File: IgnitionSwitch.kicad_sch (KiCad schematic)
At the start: 13 parts, among them J28 KILL_SW_IND, J7 BPS_PWR_OUT, J9 POW_2ND_CONN, SW8 SW_Rotary2x6, U5 EL3H7, U6 EL3H7

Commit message: Remove 12V isolator, swap CAN connector pins, etc.
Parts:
- SW8: footprint UTSVT_Special:CK1035_resized -> (none)
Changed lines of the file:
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@@
     (effects (font (size 1.27 1.27)) (justify left))
   )
-  (symbol (lib_id "Switch:SW_Rotary2x6") (at 163.83 96.52 180)
+  (symbol (lib_id "Switch:SW_Rotary2x6") (at 163.83 96.52 180) (unit 1)
     (in_bom yes) (on_board yes)
     (property "Reference" "SW8" (id 0) (at 162.56 75.565 0))
     (property "Value" "SW_Rotary2x6" (id 1) (at 162.56 77.8764 0))
-    (property "Footprint" "UTSVT_Special:CK1035_resized" (id 2) (at 166.37 111.76 0)
+    (property "Footprint" "" (id 2) (at 166.37 111.76 0)
       (effects (font (size 1.27 1.27)) hide)
     )
@@
     (pin "9")
   )
-  (symbol (lib_id "Device:R_US") (at 231.14 113.03 0)
+  (symbol (lib_id "Device:R_US") (at 231.14 113.03 0) (unit 1)
     (in_bom yes) (on_board yes)
     (property "Reference" "R12" (id 0) (at 232.8672 111.8616 0)
@@
     (pin "2")
   )
-  (symbol (lib_id "Device:LED") (at 231.14 121.92 90)
+  (symbol (lib_id "Device:LED") (at 231.14 121.92 90) (unit 1)
     (in_bom yes) (on_board yes)
     (property "Reference" "D1" (id 0) (at 234.1372 120.9294 90)
@@
     (pin "2")
   )
-  (symbol (lib_id "Connector:TestPoint") (at 137.16 82.55 0)
+  (symbol (lib_id "Connector:TestPoint") (at 137.16 82.55 0) (unit 1)
     (in_bom yes) (on_board yes)
     (property "Reference" "TP10" (id 0) (at 138.6332 79.5528 0)
@@
     (pin "1")
   )
-  (symbol (lib_id "Isolator:SFH617A-1") (at 100.33 99.06 270)
+  (symbol (lib_id "Isolator:SFH617A-1") (at 100.33 99.06 270) (unit 1)
     (in_bom yes) (on_board yes)
     (property "Reference" "U5" (id 0) (at 105.1052 97.8916 90)
@@
     (pin "4")
   )
-  (symbol (lib_id "Isolator:SFH617A-1") (at 123.19 99.06 270)
+  (symbol (lib_id "Isolator:SFH617A-1") (at 123.19 99.06 270) (unit 1)
     (in_bom yes) (on_board yes)
     (property "Reference" "U6" (id 0) (at 127.9652 97.8916 90)
@@
     (pin "4")
   )
-  (symbol (lib_id "power:GNDPWR") (at 114.3 92.71 0)
+  (symbol (lib_id "power:GNDPWR") (at 114.3 92.71 0) (unit 1)
     (in_bom yes) (on_board yes)
     (property "Reference" "#PWR0145" (id 0) (at 114.3 97.79 0)
@@
     (pin "1")
   )
-  (symbol (lib_id "power:GNDPWR") (at 91.44 92.71 0)
+  (symbol (lib_id "power:GNDPWR") (at 91.44 92.71 0) (unit 1)
     (in_bom yes) (on_board yes)
     (property "Reference" "#PWR0146" (id 0) (at 91.44 97.79 0)
@@
     (pin "1")
   )
-  (symbol (lib_id "power:GND") (at 120.65 106.68 0)
+  (symbol (lib_id "power:GND") (at 120.65 106.68 0) (unit 1)
     (in_bom yes) (on_board yes)
     (property "Reference" "#PWR0147" (id 0) (at 120.65 113.03 0)
@@
     (pin "1")
   )
-  (symbol (lib_id "power:GND") (at 97.79 106.68 0)
+  (symbol (lib_id "power:GND") (at 97.79 106.68 0) (unit 1)
     (in_bom yes) (on_board yes)
     (property "Reference" "#PWR0148" (id 0) (at 97.79 113.03 0)
@@
     (pin "1")
   )
-  (symbol (lib_id "Device:R_US") (at 106.68 113.03 0)
+  (symbol (lib_id "Device:R_US") (at 106.68 113.03 0) (unit 1)
     (in_bom yes) (on_board yes)
     (property "Reference" "R10" (id 0) (at 108.4072 111.8616 0)
@@
     (pin "2")
   )
-  (symbol (lib_id "Device:R_US") (at 129.54 113.03 0)
+  (symbol (lib_id "Device:R_US") (at 129.54 113.03 0) (unit 1)
     (in_bom yes) (on_board yes)
     (property "Reference" "R11" (id 0) (at 131.2672 111.8616 0)
@@
     (pin "2")
   )
-  (symbol (lib_id "power:+3.3V") (at 129.54 109.22 0)
+  (symbol (lib_id "power:+3.3V") (at 129.54 109.22 0) (unit 1)
     (in_bom yes) (on_board yes)
     (property "Reference" "#PWR0149" (id 0) (at 129.54 113.03 0)
@@
     (pin "1")
   )
-  (symbol (lib_id "power:+3.3V") (at 106.68 109.22 0)
+  (symbol (lib_id "power:+3.3V") (at 106.68 109.22 0) (unit 1)
     (in_bom yes) (on_board yes)
     (property "Reference" "#PWR0150" (id 0) (at 106.68 113.03 0)
@@
     (pin "1")
   )
-  (symbol (lib_id "Connector_Generic:Conn_01x02") (at 175.26 120.65 0)
+  (symbol (lib_id "Connector_Generic:Conn_01x02") (at 175.26 120.65 0) (unit 1)
     (in_bom yes) (on_board yes)
     (property "Reference" "J7" (id 0) (at 177.292 120.8532 0)
@@
     (pin "2")
   )
-  (symbol (lib_id "power:GNDPWR") (at 167.64 124.46 0)
+  (symbol (lib_id "power:GNDPWR") (at 167.64 124.46 0) (unit 1)
     (in_bom yes) (on_board yes)
     (property "Reference" "#PWR0151" (id 0) (at 167.64 129.54 0)
@@
     (pin "1")
   )
-  (symbol (lib_id "Connector_Generic:Conn_01x02") (at 255.27 106.68 0)
+  (symbol (lib_id "Connector_Generic:Conn_01x02") (at 255.27 106.68 0) (unit 1)
     (in_bom yes) (on_board yes)
     (property "Reference" "J28" (id 0) (at 257.302 106.8832 0)
@@
     (pin "2")
   )
-  (symbol (lib_id "Connector_Generic:Conn_01x02") (at 191.77 93.98 0)
+  (symbol (lib_id "Connector_Generic:Conn_01x02") (at 191.77 93.98 0) (unit 1)
     (in_bom yes) (on_board yes)
     (property "Reference" "J9" (id 0) (at 193.802 94.1832 0)
@@
     (pin "2")
   )
-  (symbol (lib_id "power:GNDPWR") (at 184.15 99.06 0)
+  (symbol (lib_id "power:GNDPWR") (at 184.15 99.06 0) (unit 1)
     (in_bom yes) (on_board yes)
     (property "Reference" "#PWR0129" (id 0) (at 184.15 104.14 0)
@@
     (pin "1")
   )
-  (symbol (lib_id "Device:R_US") (at 135.89 88.9 270)
+  (symbol (lib_id "Device:R_US") (at 135.89 88.9 270) (unit 1)
     (in_bom yes) (on_board yes)
     (property "Reference" "R6" (id 0) (at 137.0584 90.6272 0)
@@
     (pin "2")
   )
-  (symbol (lib_id "Device:R_US") (at 111.506 86.36 270)
+  (symbol (lib_id "Device:R_US") (at 111.506 86.36 270) (unit 1)
     (in_bom yes) (on_board yes)
     (property "Reference" "R5" (id 0) (at 112.6744 88.0872 0)

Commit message: Release v2.4 and gerbers
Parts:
- SW8: footprint (none) -> Connector_Molex:Molex_Micro-Fit_3.0_43045-1412_2x07_P3.00mm_Vertical
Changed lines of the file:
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@@
     (property "Reference" "SW8" (id 0) (at 162.56 75.565 0))
     (property "Value" "SW_Rotary2x6" (id 1) (at 162.56 77.8764 0))
-    (property "Footprint" "" (id 2) (at 166.37 111.76 0)
+    (property "Footprint" "Connector_Molex:Molex_Micro-Fit_3.0_43045-1412_2x07_P3.00mm_Vertical" (id 2) (at 166.37 111.76 0)
       (effects (font (size 1.27 1.27)) hide)
     )

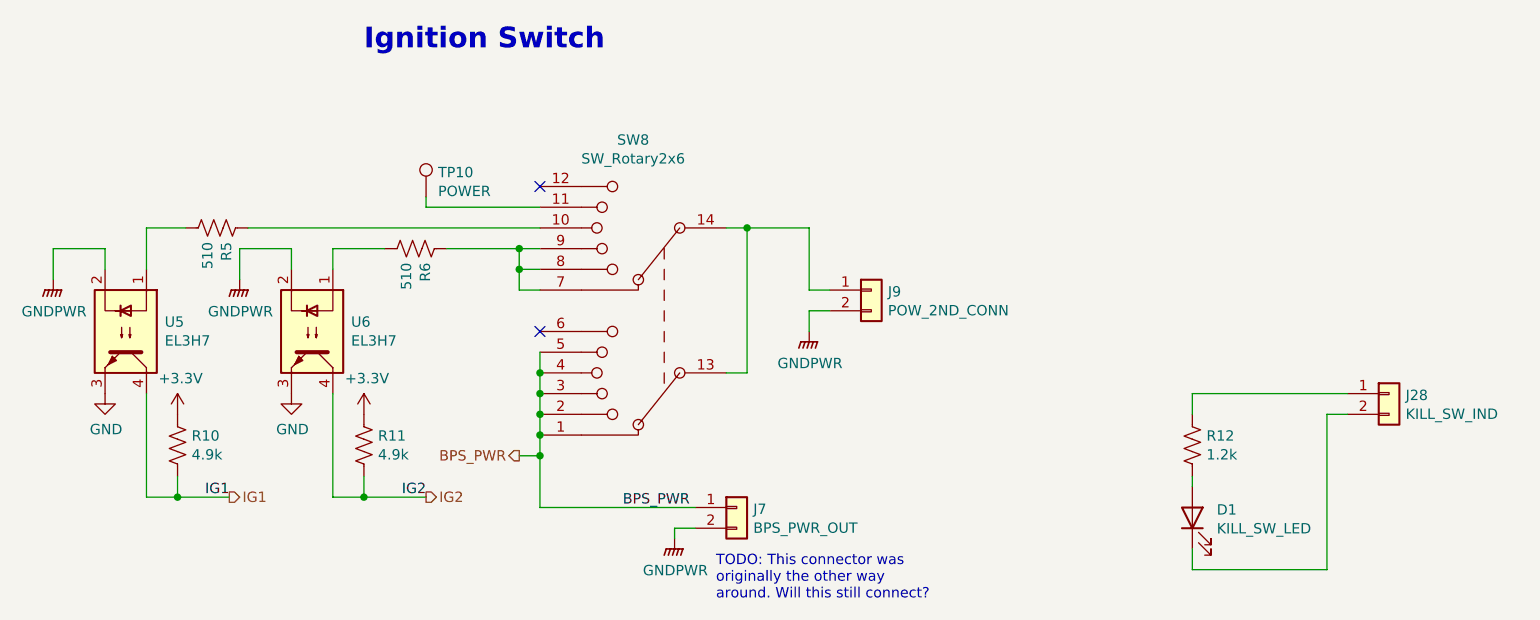
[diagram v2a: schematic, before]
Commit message: Daybreak rework (#24)
* Schematic notations for rework changes

* Updated schematic in accordance to previous weeks annotated changes

* Added .lck files to .gitignore.

* Renamed Clk to PA5, removed CAN_TX/RX test points, deleted other .lck file and #auto_saved_files# (hopefully this does not break anything.

* Changed testpoints to pin headers.

* removed camera, fixed connectors, and changed status LEDS

* Schematic finished :) hopefully not broken

* Added back lights + drivers + timer for all blinkers and brake lights

* Fuse added for motorCAN 12V

* Renamed local net labels to be different from hierarchical ones in the MinionBrdInterface so that they aren't connected. Changed Regen input to BPS Hazard light since we aren't using regen but will be alerting the driver of BPS faults.

* Flipped optoisolators, changed resistor values, added second connector to motor can and disconnected shield pins for now since I haven't seen them used (will chack against old version to see what the circuit looked like), copied power-in circuit from contactor board, added optoisolator to timer and blinker light connection.

* Changed names and added power flags until KiCAD ERC was satisfied. Hopefully this did not involve doing anything that wasn't supposed to be done.

* Added UTSVT libraries to the gitignore.

* Added footprints. I think this is everything except the fuse.

* Fuse footprint added and blinker changed to software

* Started cleaning some comments, changed EL3H7 data sheet link, removed extra motor CAN connector and changed original one to match (I think) motor controller connector, removed extra mounting holes, removed hierarchical power labels.

* renamed power state indicators to contactors and removed unused contactors, added current limiting resistors to lights drivers, changed mosfet to new mosfet

* Updated contactor pins.

* added circuitry for limit switch brake, added mosfet to drive LEDs, cleaned up legacy comments, 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
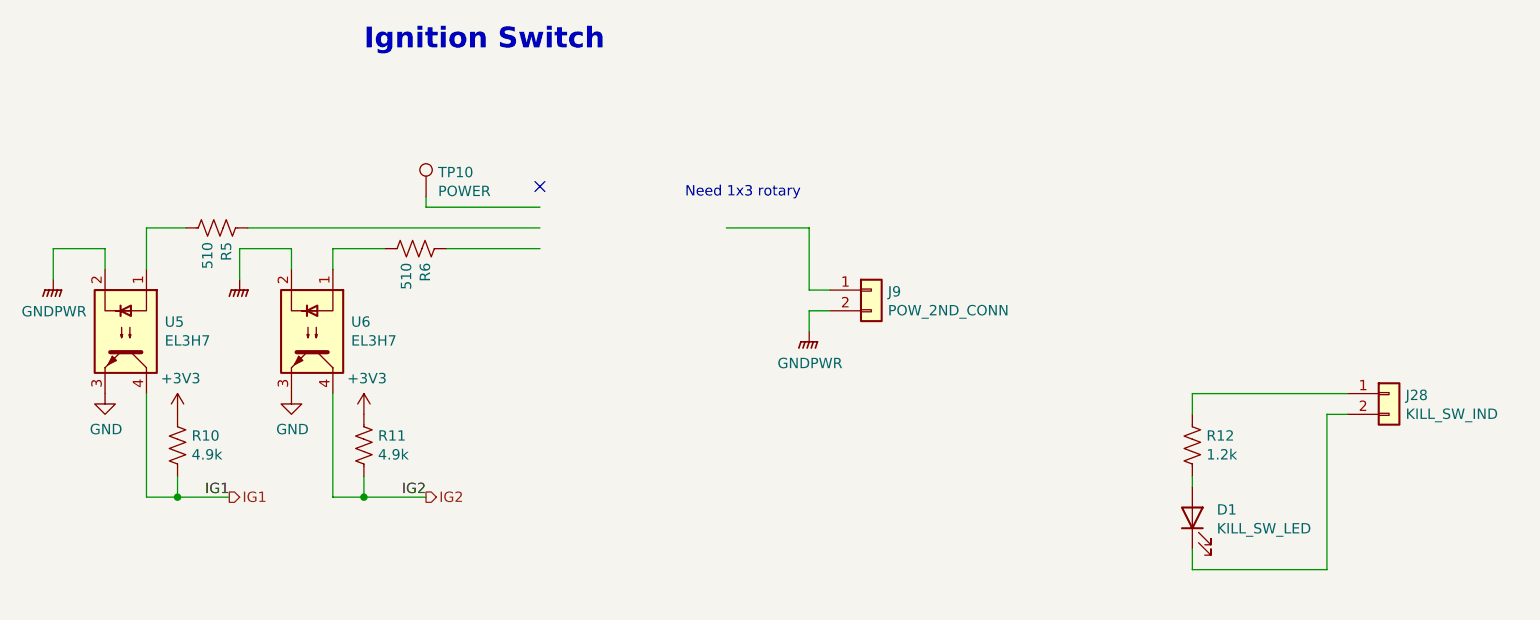
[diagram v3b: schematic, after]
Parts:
- removed J7: BPS_PWR_OUT, UTSVT_Connectors:Molex_MicroFit3.0_1x2xP3.00mm_PolarizingPeg_Vertical, symbol Connector_Generic:Conn_01x02
- removed SW8: SW_Rotary2x6, Connector_Molex:Molex_Micro-Fit_3.0_43045-1412_2x07_P3.00mm_Vertical, symbol Switch:SW_Rotary2x6
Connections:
- no-connect marks 2 -> 1
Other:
- note added: "Need 1x3 rotary"
- note removed: "TODO: This connector was originally the other way around. Will this still connect?"
